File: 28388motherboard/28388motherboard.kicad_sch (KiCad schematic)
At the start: 103 parts, among them CN1 DB141V-2.54-6P, CN2 DB141V-2.54-6P, J1 Conn_02x02_Top_Bottom, J10 PM2.54-2*10, J11 Conn_02x10_Top_Bottom, J12 Conn_02x10_Top_Bottom, J13 Conn_02x02_Counter_Clockwise, J14 Conn_02x02_Counter_Clockwise, J15 2.54-2*5, J16 2.54-2*5, J18 Conn_02x12_Odd_Even, J6 Conn_02x02_Top_Bottom, J9 2.54-2*5, Q1 TPT1042VQ-SO1R-S, Q2 TPT1042VQ-SO1R-S, Q5 SN74LVC14APWRG4, Q6 SN74LVC14APWRG4, Q7 FMMT618TA, Q8 AMS1117-3.3, Q9 FMMT618TA, X1 20MHz, X2 20MHz

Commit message: 1. 485 缺电源+5V 1 2. 标一下已用ADCforDCbus 1 3. 逆变器三相采样 coming soon 4. 电源灯 5V 3.3V 1 5. 测试点 1 6. 电源走线 需要人检查 7. 接口附近储能电容 1 8.
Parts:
- added C107, C109: 1uF, Capacitor_SMD:C_0402_1005Metric, symbol Device:C_Small
- added C108, C110: 0.1uF, Capacitor_SMD:C_0402_1005Metric, symbol Device:C_Small
- added D34, D35: LEDRED, LED_SMD:LED_0805_2012Metric, symbol sheet1-altium-import:root_3_LED0
- added R188: 1K, Resistor_SMD:R_0805_2012Metric, symbol sheet1-altium-import:root_1_Res2
- added R189: 2K, Resistor_SMD:R_0805_2012Metric, symbol sheet1-altium-import:root_1_Res2
- added TP_5V1, TP_5V8, TP_5V9, TP_CANEN1, TP_CANEN2, TP_CANH1, TP_CANH2, TP_CANL1, TP_CANL2, TP_CANRX1, TP_CANRX2, TP_CANTX1, TP_CANTX2, TP_CK1, TP_CK2, TP_CK3, TP_CK4, TP_CL1, TP_CL2, TP_CLK1, TP_CLK2, TP_DA1, TP_DA2, TP_G10, TP_G7, TP_G8, TP_G9, TP_MI1, TP_MI2, TP_MI3, TP_MI4, TP_MO1, TP_MO2, TP_MO3, TP_MO4, TP_PWM1A1, TP_PWM1B1, TP_PWM2A1, TP_PWM2B1, TP_PWM3A1, TP_PWM3B1, TP_PWM4A1, TP_PWM4B1, TP_PWM5A1, TP_PWM5B1, TP_PWM6A1, TP_PWM6B1, TP_RX2, TP_RX3, TP_RX4, TP_RX5, TP_STE1, TP_STE2, TP_STE3, TP_STE4, TP_TX1, TP_TX2, TP_TX3, TP_TX4, TP_VDD1, TP_WR1, TP_WR2, TP_WR3, TP_WR4: TestPoint, TestPoint:TestPoint_Pad_1.0x1.0mm, symbol Connector:TestPoint
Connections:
- net 485_RTS_1: now also TP_WR1.1
- net 485_RTS_2: now also TP_WR2.1
- net 485_RTS_3: now also TP_WR3.1
- net 485_RTS_4: now also TP_WR4.1
- net ADC_CLK_X1: now also TP_CLK1.1
- net ADC_CLK_X2: now also TP_CLK2.1
- net CAN_H1: now also TP_CANH1.1
- net CAN_H2: now also TP_CANH2.1
- net CAN_L1: now also TP_CANL1.1
- net CAN_L2: now also TP_CANL2.1
- net D+5V: now also D34.1 (A), TP_5V8.1, TP_5V9.1
- net DSP-PWM1A: now also TP_PWM1A1.1
- net DSP-PWM1B: now also TP_PWM1B1.1
- net DSP-PWM2A: now also TP_PWM2A1.1
- net DSP-PWM2B: now also TP_PWM2B1.1
- net DSP-PWM3A: now also TP_PWM3A1.1
- net DSP-PWM3B: now also TP_PWM3B1.1
- net DSP-PWM4A: now also TP_PWM4A1.1
- net DSP-PWM4B: now also TP_PWM4B1.1
- net DSP-PWM5A: now also TP_PWM5A1.1
- net DSP-PWM5B: now also TP_PWM5B1.1
- net DSP-PWM6A: now also TP_PWM6A1.1
- net DSP-PWM6B: now also TP_PWM6B1.1
- net DSP_A_CAN_EN: now also TP_CANEN1.1
- net DSP_A_CAN_RX: now also TP_CANRX1.1
- net DSP_A_CAN_TX: now also TP_CANTX1.1
- net DSP_B_CAN_EN: now also TP_CANEN2.1
- net DSP_B_CAN_RX: now also TP_CANRX2.1
- net DSP_B_CAN_TX: now also TP_CANTX2.1
- net GND: now also C107.2, C108.2, C109.2, C110.2, R188.1, R189.1, TP_G10.1, TP_G7.1, TP_G8.1, TP_G9.1
- net GPIO100: now also TP_MO2.1
- net GPIO101: now also TP_MI2.1
- net GPIO102: now also TP_CK2.1
- net GPIO103: now also TP_STE2.1
- net GPIO104: now also TP_TX4.1
- net GPIO105: now also TP_RX5.1
- net GPIO137: now also TP_TX2.1
- net GPIO138: now also TP_RX3.1
- net GPIO24: now also TP_MO1.1
- net GPIO25: now also TP_MI1.1
- net GPIO26: now also TP_CK1.1
- net GPIO27: now also TP_STE1.1
- net GPIO32: now also TP_DA1.1
- net GPIO33: now also TP_CL1.1
- net GPIO34: now also TP_DA2.1
- net GPIO35: now also TP_CL2.1
- net GPIO48: now also TP_TX1.1
- net GPIO49: now also TP_RX2.1
- net GPIO58: now also TP_MO4.1
- net GPIO59: now also TP_CK4.1
- net GPIO60: now also TP_STE4.1
- net GPIO61: now also TP_MI4.1
- net GPIO89: now also TP_TX3.1
- net GPIO90: now also TP_RX4.1
- net GPIO91: now also TP_MO3.1
- net GPIO92: now also TP_MI3.1
- net GPIO93: now also TP_CK3.1
- net GPIO94: now also TP_STE3.1
- net Header-D+5V: now also TP_5V1.1
- net VDD: now also C107.1, C108.1, C109.1, C110.1, D35.1 (A), TP_VDD1.1
- new net: D34.2 (K), R188.2
- new net: D35.2 (K), R189.2
- no-connect marks 25 -> 45
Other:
- note added: "485 for tformat"
- note added: "电源提示灯"
- note removed: "H485接Unitree A1关节模组"

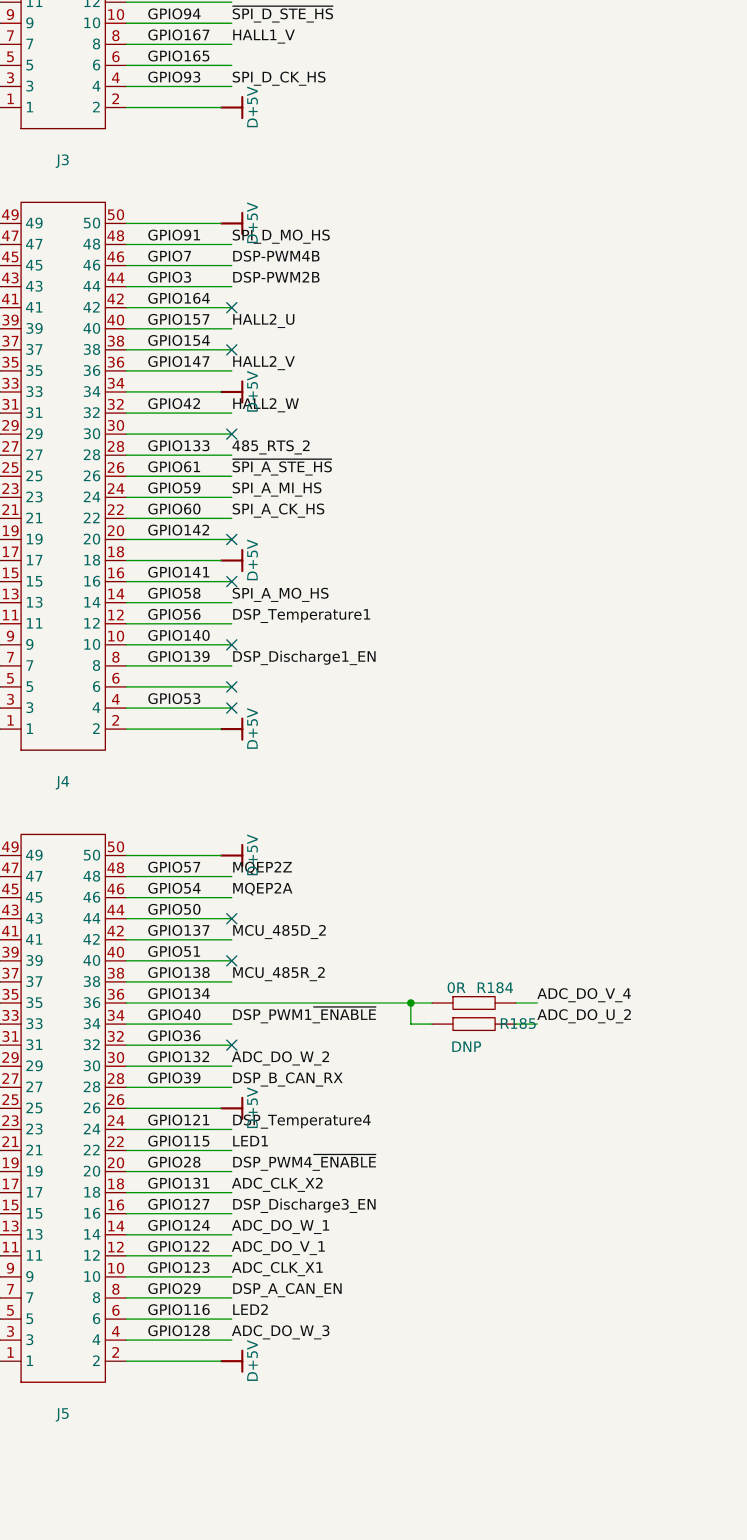
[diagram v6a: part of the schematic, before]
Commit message: [2026.03.01]底板调整泪滴后准备下单
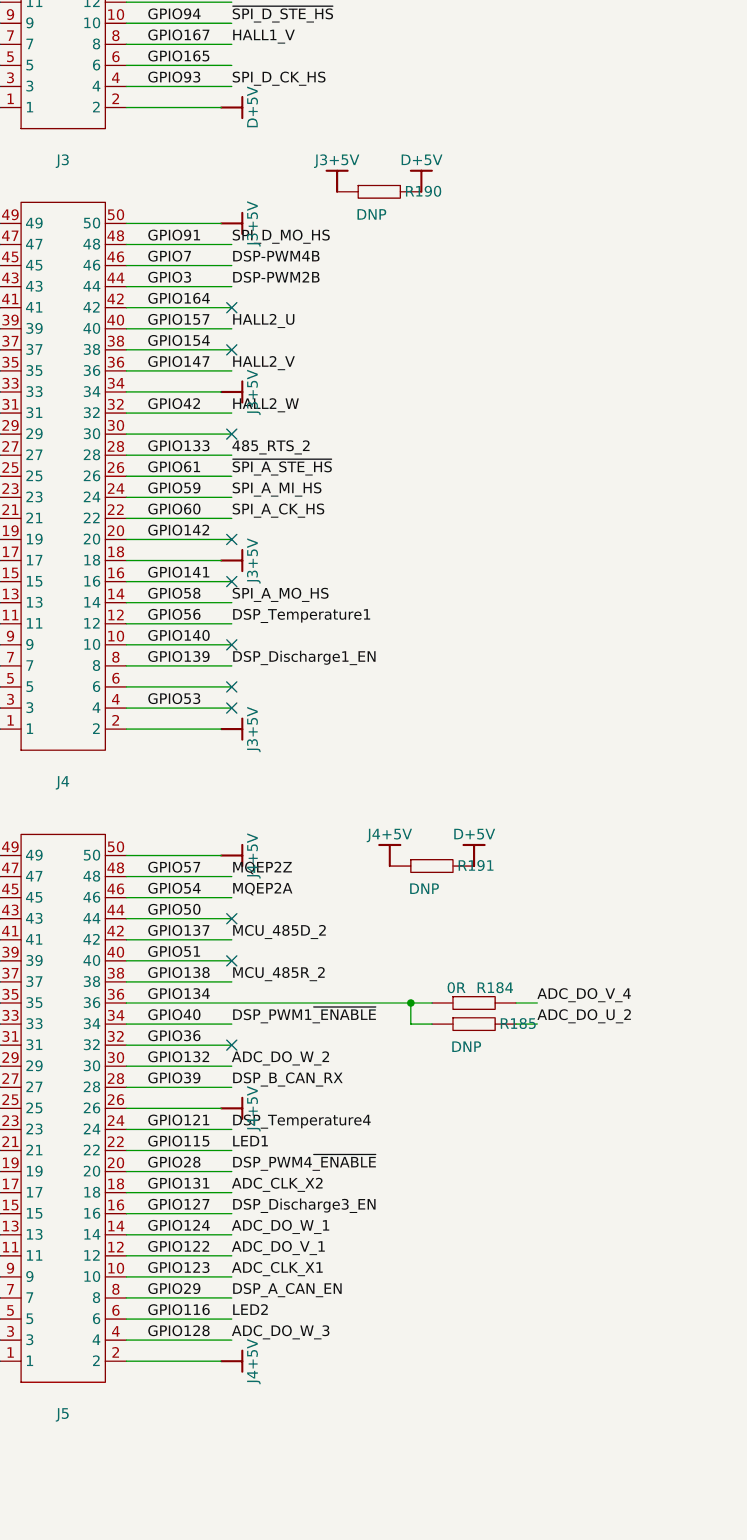
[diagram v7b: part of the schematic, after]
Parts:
- added R190, R191: DNP, Lib_sheet_10:R_0603_1608Metric, symbol sheet1-altium-import:RES_2
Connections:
- net D+5V: now also R190.2, R191.2; no longer J4.18, J4.2, J4.34, J4.50, J5.2, J5.26, J5.50
- new net J3+5V: J4.18, J4.2, J4.34, J4.50, R190.1
- new net J4+5V: J5.2, J5.26, J5.50, R191.1

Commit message: 修改部分丝印和添加部分测试点，todo: 修改电源接口、dac接口、电源走线、I2C布局
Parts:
- added TP_G1, TP_G2, TP_G3: TestPoint, TestPoint:TestPoint_Pad_1.0x1.0mm, symbol Connector:TestPoint
- renumbered TP_RX2 to TP_RX1, TP_RX3 to TP_RX2, TP_RX4 to TP_RX3, TP_RX5 to TP_RX4
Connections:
- net GND: now also TP_G1.1, TP_G2.1, TP_G3.1
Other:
- note added: "ADC 14"
- note added: "ADC 15"
- note added: "ADC A0"
- note added: "ADC A1"
- note added: "ADC A2"
- note added: "ADC A3"
- note added: "ADC A4"
- note added: "ADC A5"
- note added: "ADC B0"
- note added: "ADC B1"
- note added: "ADC B2"
- note added: "ADC B3"
- note added: "ADC B4"
- note added: "ADC B5"
- note added: "ADC C2"
- note added: "ADC C3"
- note added: "ADC C4"
- note added: "ADC C5"
- note added: "ADC D0"
- note added: "ADC D1"
- note added: "ADC D2"
- note added: "ADC D3"
- note added: "ADC D4"
- note added: "ADC D5"
